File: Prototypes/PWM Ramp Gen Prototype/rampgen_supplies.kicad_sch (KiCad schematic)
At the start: 45 parts, among them U10 BD50FC0FP-E2, U11 BD50FC0FP-E2, U12 BD33FC0FP-E2, U13 REF3433TIDBVR, U7 TLV3502, U9 AD8602

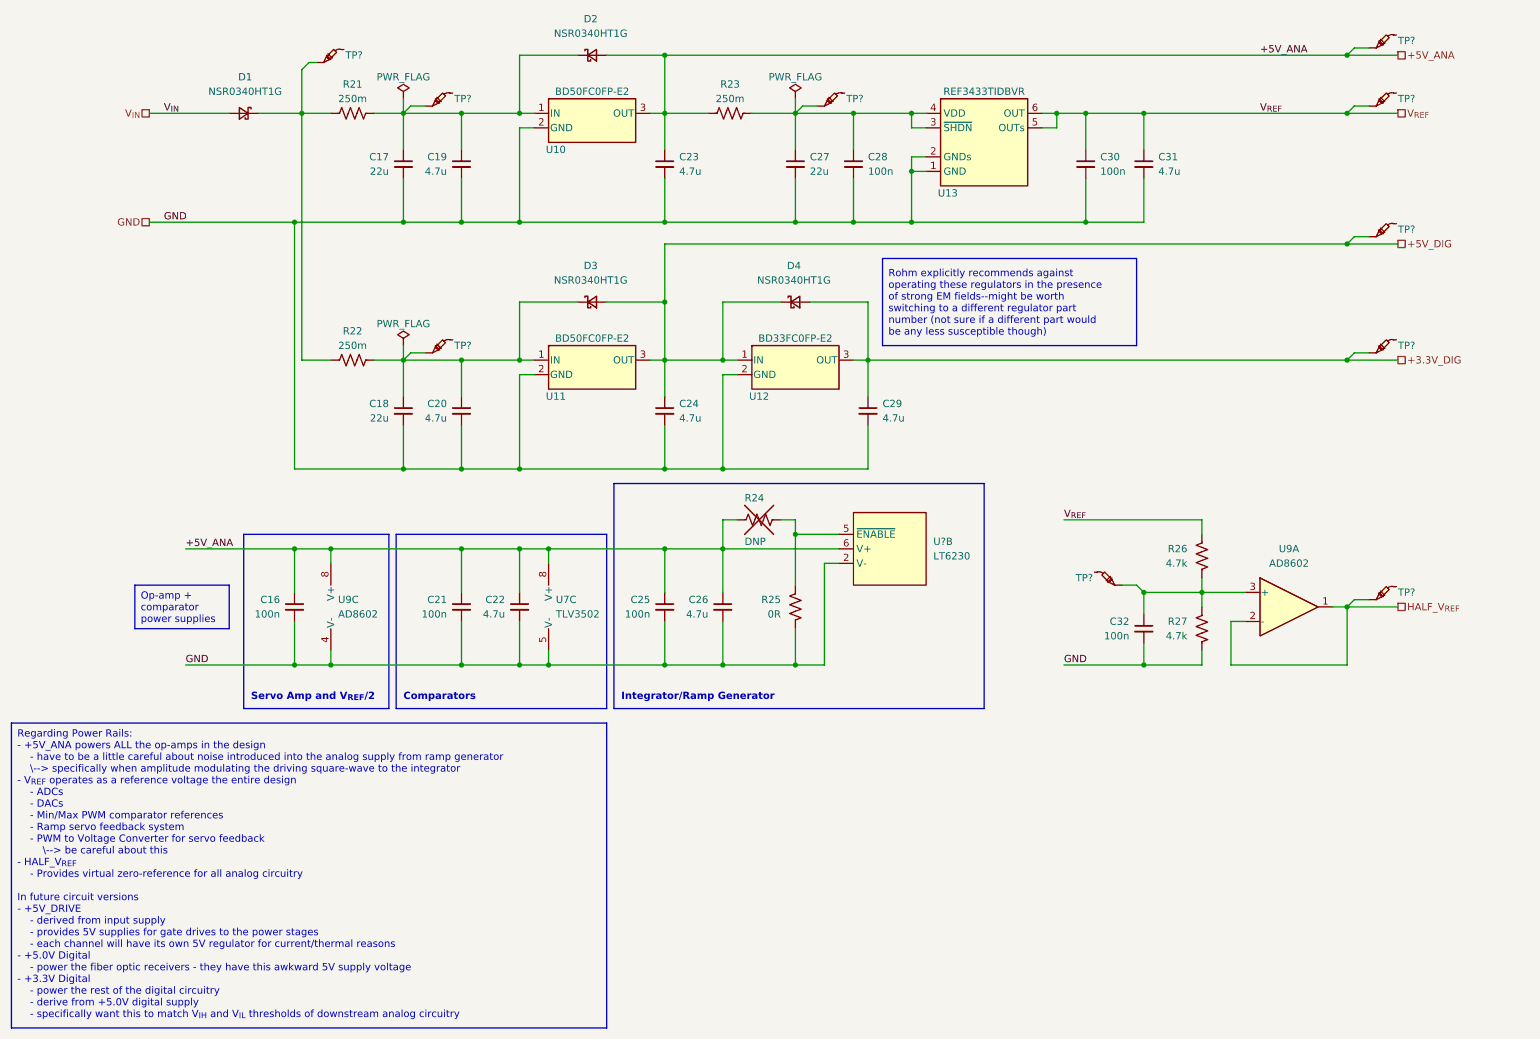
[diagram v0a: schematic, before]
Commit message: Comparator and Op-amp tweaks for BOM consolidation; final layout
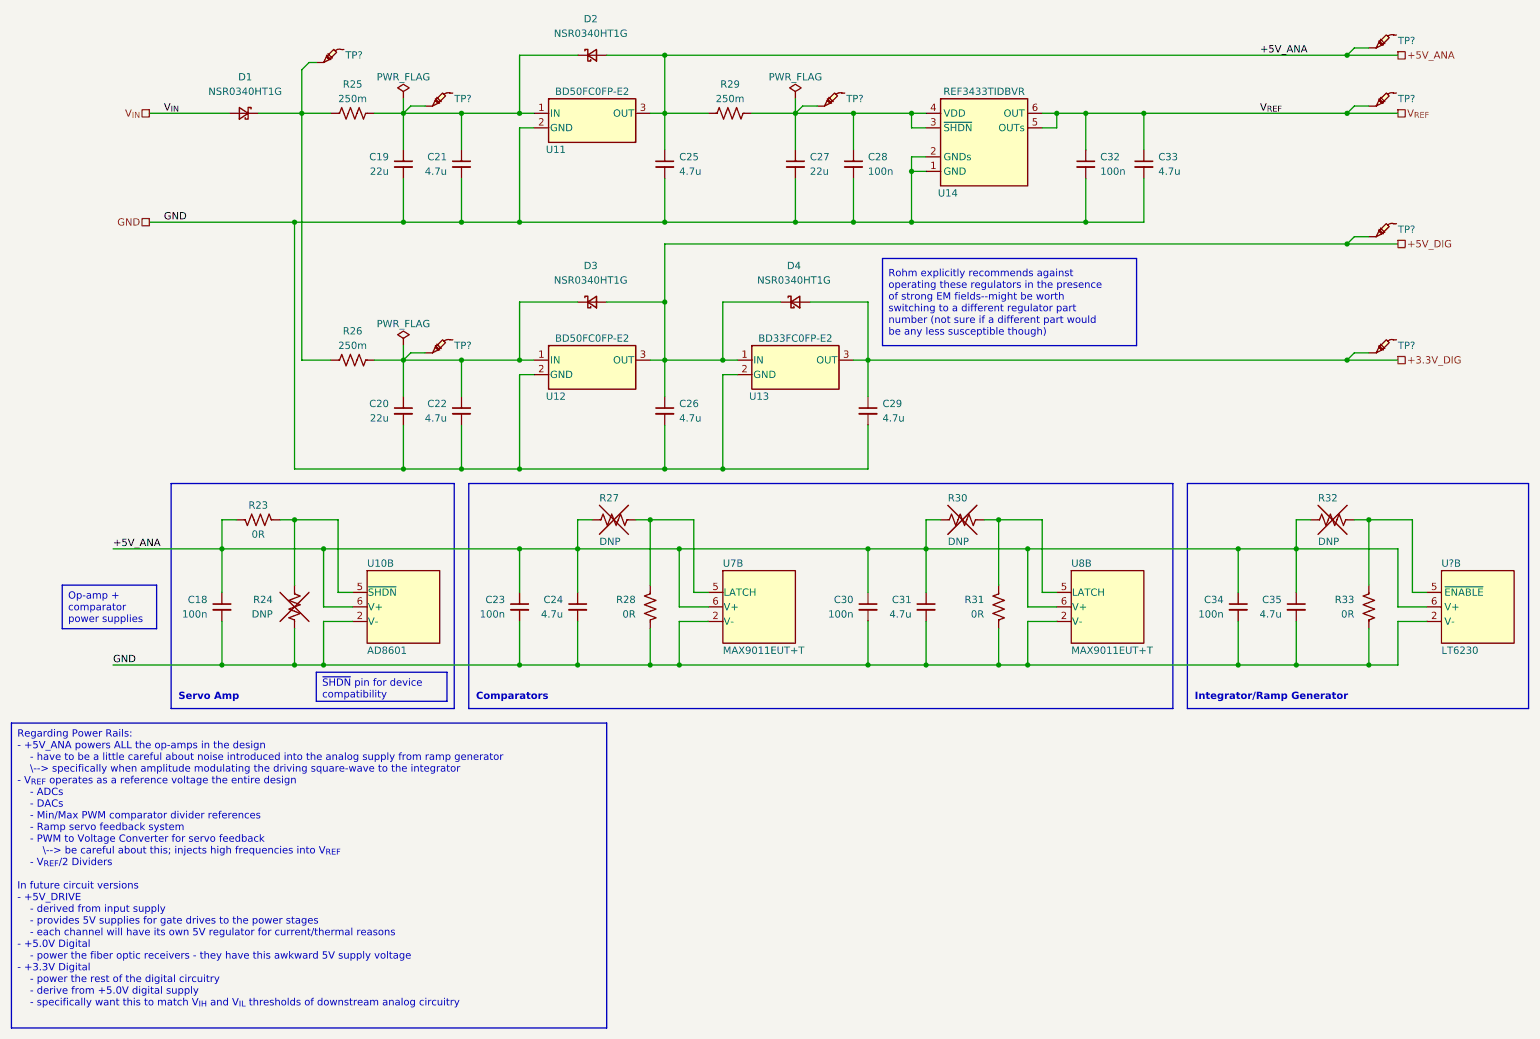
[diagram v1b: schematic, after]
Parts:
- removed C21, C32: 100n, Capacitor_SMD:C_0603_1608Metric_Pad1.08x0.95mm_HandSolder, symbol Custom-Capacitor:CL10B104KB8NNWC
- removed C22: 4.7u, Capacitor_SMD:C_0805_2012Metric_Pad1.18x1.45mm_HandSolder, symbol Custom-Capacitor:CL21A475KLCLQNC
- removed R26, R27: 4.7k, Resistor_SMD:R_0603_1608Metric_Pad0.98x0.95mm_HandSolder, symbol Custom-Resistor:RMCF0603FT4K70
- removed TP? (x2): -, TestPoint:TestPoint_Pad_D2.0mm, symbol Custom-LogicIC:TestPoint
- removed U7: TLV3502, Package_SO:SOIC-8_3.9x4.9mm_P1.27mm, symbol Custom-AnalogIC:TLV3502
- removed U9: AD8602, Package_SO:MSOP-8_3x3mm_P0.65mm, symbol Custom-AnalogIC:AD8602
- added C23, C30: 100n, Capacitor_SMD:C_0603_1608Metric_Pad1.08x0.95mm_HandSolder, symbol Custom-Capacitor:CL10B104KB8NNWC
- added C24, C31: 4.7u, Capacitor_SMD:C_0805_2012Metric_Pad1.18x1.45mm_HandSolder, symbol Custom-Capacitor:CL21A475KLCLQNC
- added R23, R28, R31: 0R, Resistor_SMD:R_0603_1608Metric_Pad0.98x0.95mm_HandSolder, symbol Custom-Resistor:RMCF0603ZT0R00
- added R24, R27, R30: DNP, Custom-RLC:DNP_R_0603_1608Metric_Pad0.98x0.95mm_HandSolder, symbol Custom-Resistor:JUMPER_DNP
- added U10: AD8601, Package_TO_SOT_SMD:SOT-23-6_Handsoldering, symbol Custom-AnalogIC:AD8601
- added U7, U8: MAX9011EUT+T, Package_TO_SOT_SMD:SOT-23-6_Handsoldering, symbol Custom-AnalogIC:MAX9011
- renumbered C16 to C18, C17 to C19, C18 to C20, C19 to C21, C20 to C22, C23 to C25, C24 to C26, C30 to C32, C31 to C33, C25 to C34, C26 to C35, R21 to R25, R22 to R26, R23 to R29, R24 to R32, R25 to R33, U10 to U11, U11 to U12, U12 to U13, U13 to U14
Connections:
- net +5V_ANA: now also C23.1, C24.1, C30.1, C31.1, R23.2, R27.1, R30.1, U10.6 (V+), U7.6 (V+), U8.6 (V+)
- net GND: now also C23.2, C24.2, C30.2, C31.2, R24.2, R28.1, R31.1, U10.2 (V-), U7.2 (V-), U8.2 (V-)
- new net: R27.2, R28.2, U7.5 (LATCH)
- new net: R23.1, R24.1, U10.5 (~{SHDN})
- new net: R30.2, R31.2, U8.5 (LATCH)
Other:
- note added: "Servo Amp"
- note removed: "Servo Amp and V_{REF}/2"
- moved on the sheet: C18, C34, C35, R32, R33, U?B
